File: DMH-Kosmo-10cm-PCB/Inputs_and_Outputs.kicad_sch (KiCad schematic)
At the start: 0 parts

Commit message: Added initial jacks and connectors to PCBs
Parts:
- added J1, J2, J3, J5: TS_Jack_6.35mm_Sw, SynthStuff:CUI_MJ-63052A, symbol SynthStuff:TS_Jack_6.35mm_Sw
- added J200: IDC_02x05, SynthStuff:IDC-Header_2x05_P2.54mm_Vertical_BackBone, symbol SynthStuff:BackBone_Connector_10Pin
- added J50, J60: Conn_01x06, Connector_PinSocket_2.54mm:PinSocket_1x06_P2.54mm_Vertical, symbol Connector_Generic:Conn_01x06

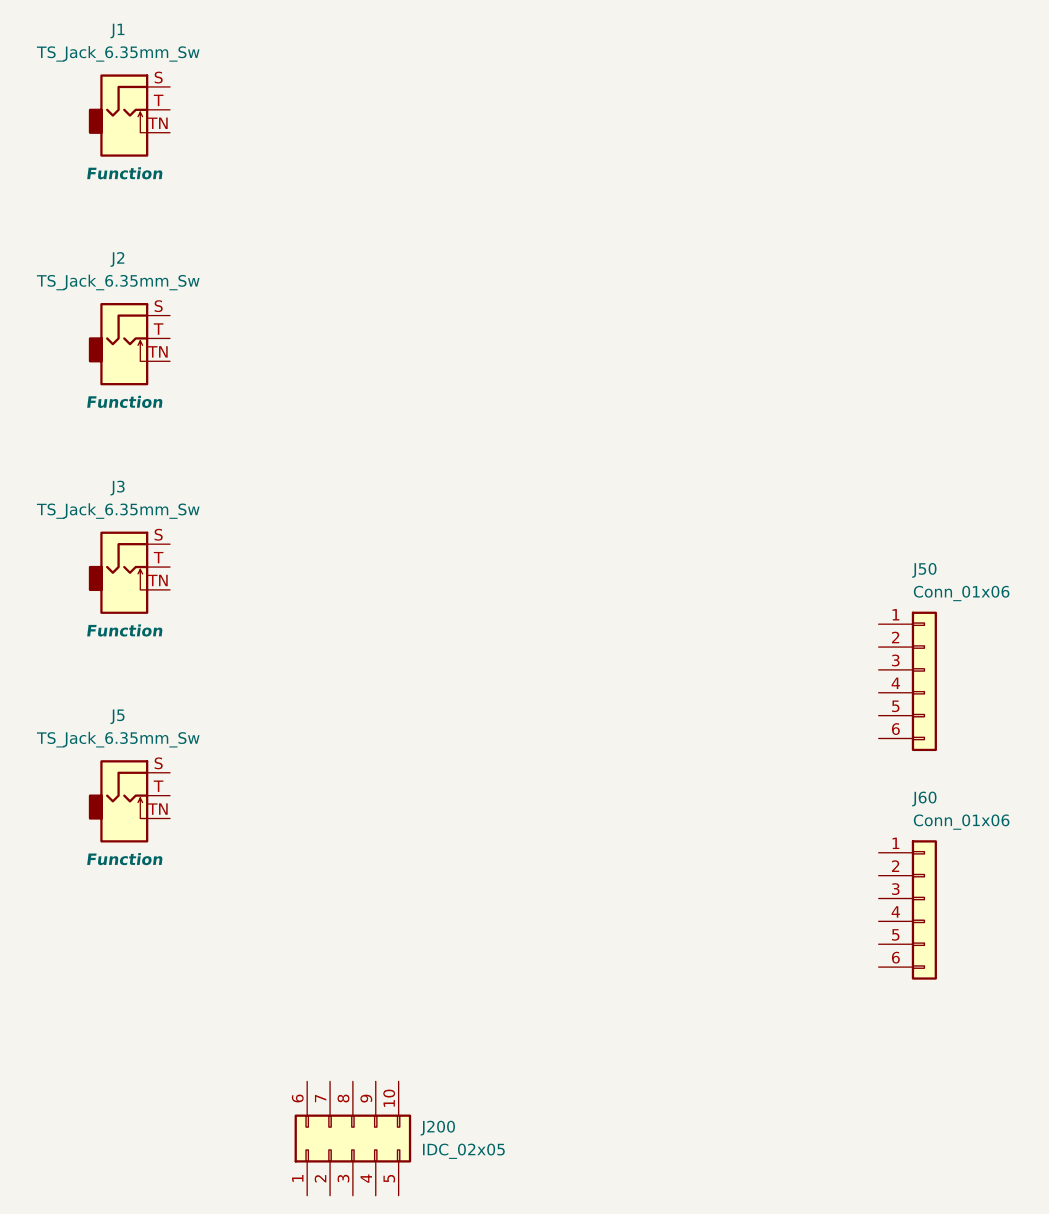
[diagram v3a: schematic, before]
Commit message: Enlarged PCB limits
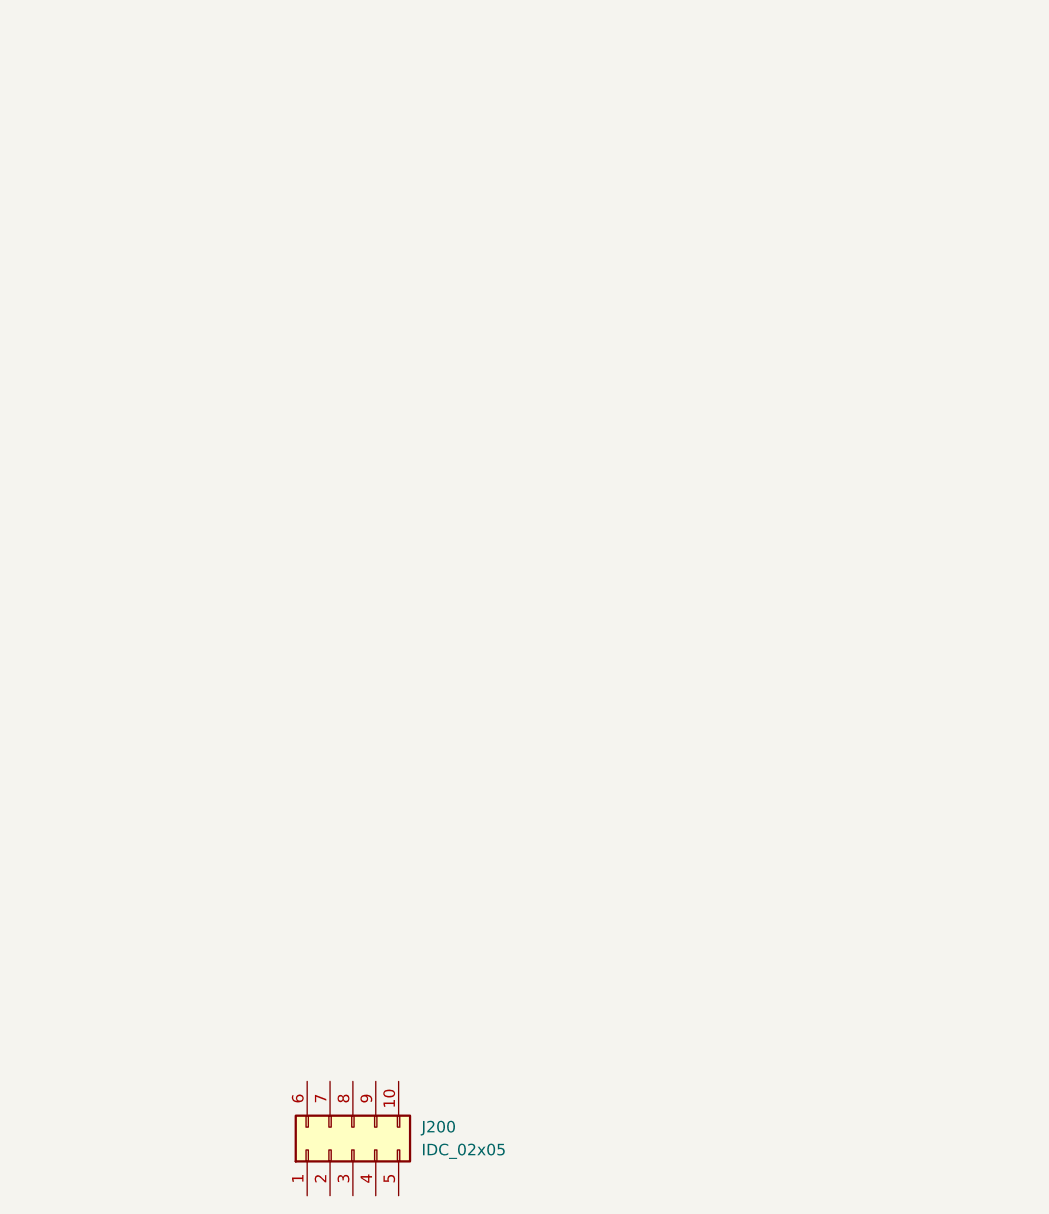
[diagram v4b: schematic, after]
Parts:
- removed J1, J2, J3, J5: TS_Jack_6.35mm_Sw, SynthStuff:CUI_MJ-63052A, symbol SynthStuff:TS_Jack_6.35mm_Sw
- removed J50, J60: Conn_01x06, Connector_PinSocket_2.54mm:PinSocket_1x06_P2.54mm_Vertical, symbol Connector_Generic:Conn_01x06
